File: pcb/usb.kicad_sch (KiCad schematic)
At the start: 7 parts, among them J2 USB_C_Receptacle_USB2.0_14P, U5 CP2102N-Axx-xQFN24

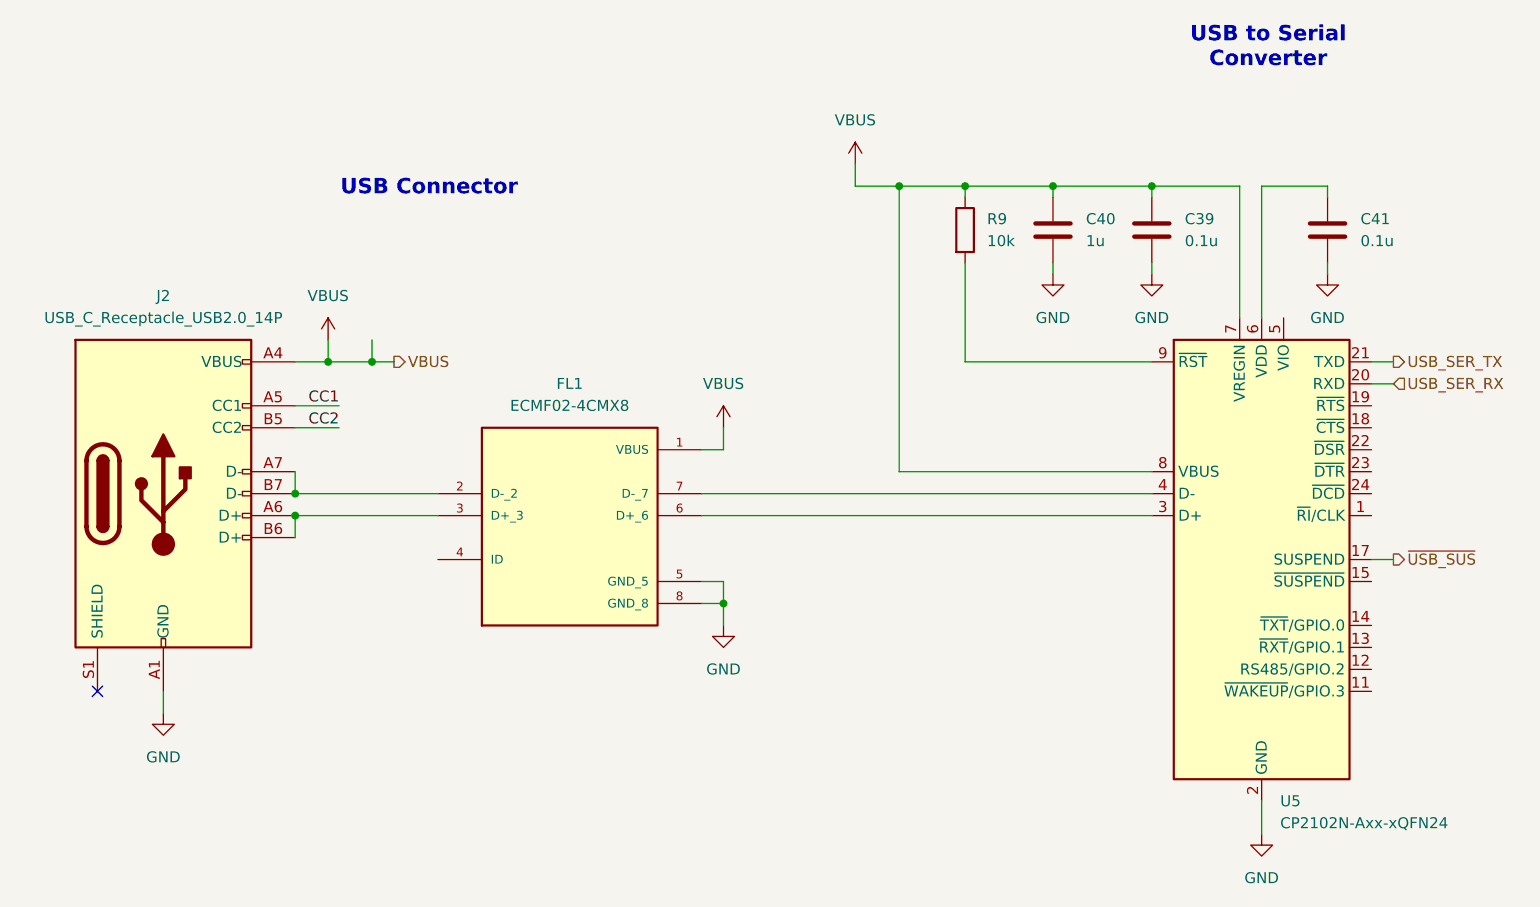
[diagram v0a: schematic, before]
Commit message: Fix display sch
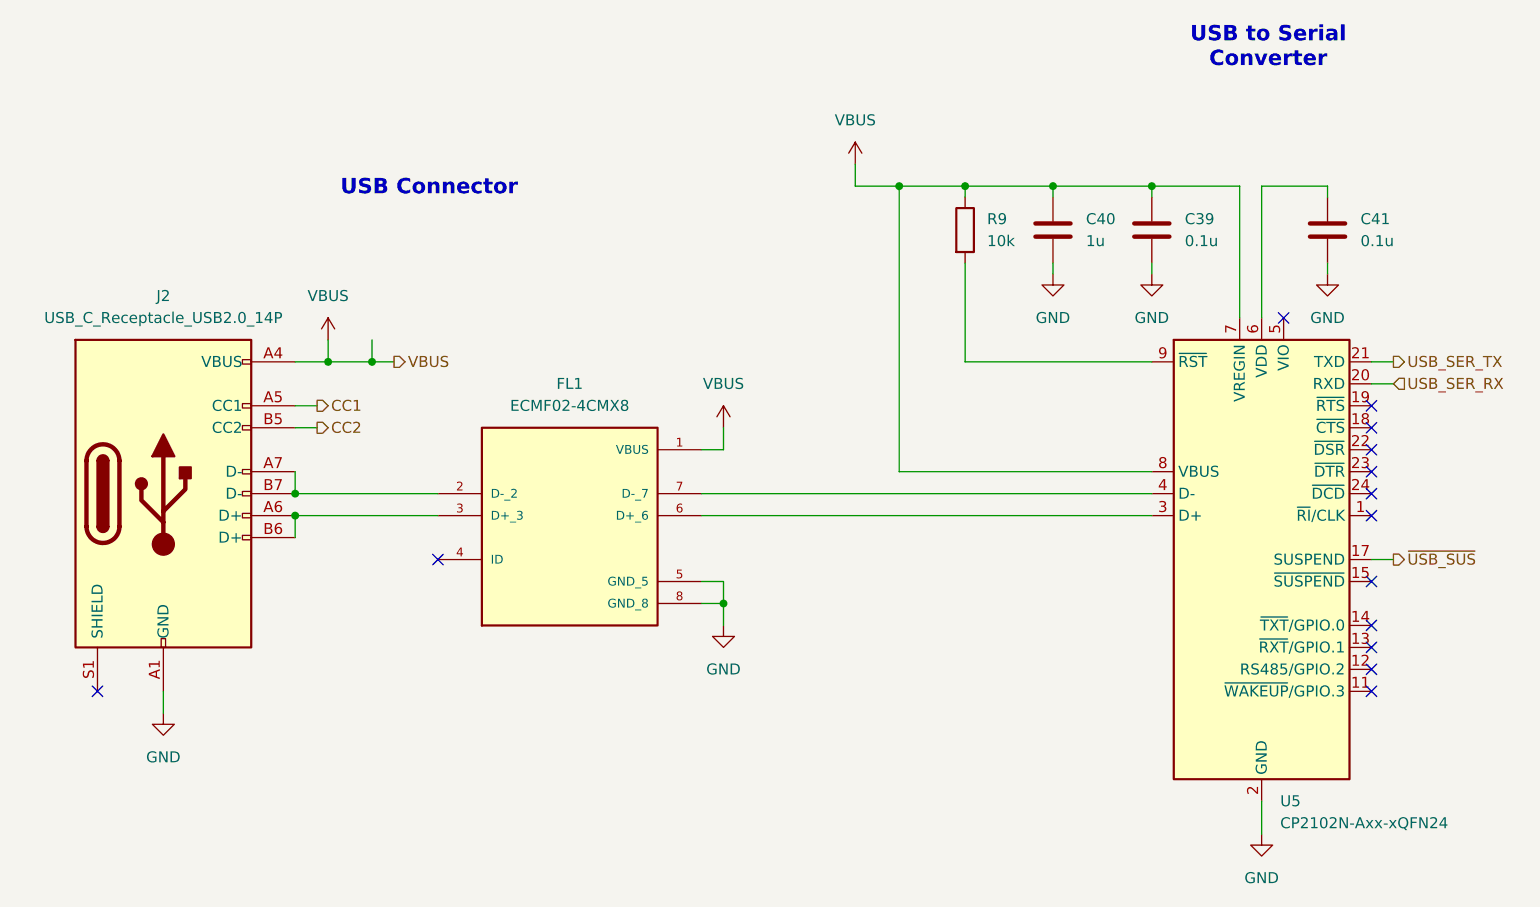
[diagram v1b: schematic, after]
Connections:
- no-connect marks 1 -> 14
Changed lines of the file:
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@@
 		(at 76.2 118.11)
 	)
+	(no_connect
+		(at 223.52 110.49)
+	)
+	(no_connect
+		(at 223.52 95.25)
+	)
+	(no_connect
+		(at 223.52 92.71)
+	)
+	(no_connect
+		(at 223.52 115.57)
+	)
+	(no_connect
+		(at 223.52 105.41)
+	)
+	(no_connect
+		(at 223.52 87.63)
+	)
+	(no_connect
+		(at 213.36 74.93)
+	)
+	(no_connect
+		(at 223.52 118.11)
+	)
+	(no_connect
+		(at 223.52 85.09)
+	)
+	(no_connect
+		(at 223.52 113.03)
+	)
+	(no_connect
+		(at 115.57 102.87)
+	)
+	(no_connect
+		(at 223.52 90.17)
+	)
+	(no_connect
+		(at 223.52 97.79)
+	)
 	(wire
 		(pts
@@
 	(wire
 		(pts
-			(xy 99.06 85.09) (xy 104.14 85.09)
-		)
-		(stroke
-			(width 0)
-			(type default)
-		)
-	)
-	(wire
-		(pts
 			(xy 223.52 102.87) (xy 226.06 102.87)
 		)
@@
 	(wire
 		(pts
+			(xy 99.06 87.63) (xy 101.6 87.63)
+		)
+		(stroke
+			(width 0)
+			(type default)
+		)
+	)
+	(wire
+		(pts
 			(xy 198.12 68.58) (xy 198.12 69.85)
 		)
@@
 	(wire
 		(pts
-			(xy 99.06 87.63) (xy 104.14 87.63)
+			(xy 99.06 85.09) (xy 101.6 85.09)
 		)
 		(stroke
@@
 		)
 	)
-	(label "CC2"
-		(at 104.14 87.63 180)
+	(hierarchical_label "CC1"
+		(shape output)
+		(at 101.6 85.09 0)
 		(effects
 			(font
 				(size 1.27 1.27)
 			)
-			(justify right bottom)
-		)
-	)
-	(label "CC1"
-		(at 104.14 85.09 180)
-		(effects
-			(font
-				(size 1.27 1.27)
-			)
-			(justify right bottom)
+			(justify left)
 		)
 	)
@@
 		(effects
 			(font
+				(size 1.27 1.27)
+			)
+			(justify left)
+		)
+	)
+	(hierarchical_label "CC2"
+		(shape output)
+		(at 101.6 87.63 0)
+		(effects
+			(font

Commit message: clean up
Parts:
- C39, C40, C41: footprint (none) -> Capacitor_SMD:C_0603_1608Metric
- R9: footprint (none) -> Resistor_SMD:R_0603_1608Metric
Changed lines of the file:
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@@
 			)
 		)
-		(property "Footprint" ""
+		(property "Footprint" "Capacitor_SMD:C_0603_1608Metric"
 			(at 187.6552 68.58 0)
 			(effects
@@
 			)
 		)
-		(property "Footprint" ""
+		(property "Footprint" "Capacitor_SMD:C_0603_1608Metric"
 			(at 219.4052 68.58 0)
 			(effects
@@
 			)
 		)
-		(property "Footprint" ""
+		(property "Footprint" "Capacitor_SMD:C_0603_1608Metric"
 			(at 199.0852 68.58 0)
 			(effects
@@
 			)
 		)
-		(property "Footprint" ""
+		(property "Footprint" "Resistor_SMD:R_0603_1608Metric"
 			(at 174.752 64.77 90)
 			(effects
